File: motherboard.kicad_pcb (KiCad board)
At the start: 2 copper layers, 100.9 x 70.4 mm, 153 parts, among them J1 USB_C_Receptacle_USB2.0, J10 Power input, J11 Bed, J12 Hotend, J13 X_LIMIT, J14 Y_LIMIT, J15 Z_LIMIT, J2 SWD, J3 EXP, J5 Conn_01x03, J6 FAN, J7 Conn_02x03_Odd_Even, J8 BED_TEMP, J9 HOTEND_TEMP, M1 NEMA17, M2 NEMA17, M3 NEMA17, M4 NEMA17, Q1 BC847, Q2 BC847, Q3 AO3400A, Q5 APM4010, Q6 APM4010, U1 MP1584, U2 STM32F103C8Tx, U3 AMS1117-3.3, U4 A4988, U5 A4988, U6 A4988, U7 A4988, U8 CH340E, Y1 8MHz

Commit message: change PCB design
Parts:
- removed the C50 at (121.2, 121.4)
- removed the C51 at (120.7, 124.2)
- removed the C52 at (113.3, 121.4)
- removed the D5 at (113.3, 128.9)
- removed D7: LED, LED_SMD:LED_0603_1608Metric_Pad1.05x0.95mm_HandSolder
- removed the R24 at (82.8, 117.4)
- removed the R26 at (103.2, 117.5)
- removed the R40 at (115.7, 125.1)
- removed the R54 at (117.7, 114.7)
- removed the REF** at (64.2, 133.8)
- removed the U2 at (99.2, 140.0)
- added C3: 4u7, Capacitor_SMD:C_0603_1608Metric_Pad1.08x0.95mm_HandSolder, F.Cu at (102.5, 146.1)
- added C35: 1n, Capacitor_SMD:C_0603_1608Metric_Pad1.08x0.95mm_HandSolder, F.Cu at (126.8, 111.8)
- added C36: 1n, Capacitor_SMD:C_0603_1608Metric_Pad1.08x0.95mm_HandSolder, F.Cu at (123.2, 125.0)
- added C41: 1u, Capacitor_SMD:C_0603_1608Metric_Pad1.08x0.95mm_HandSolder, F.Cu at (121.2, 115.5)
- added D6: LED, LED_SMD:LED_0603_1608Metric_Pad1.05x0.95mm_HandSolder, F.Cu at (117.7, 125.5)
- added GND: TestPoint_Loop_D1.80mm_Drill1.0mm_Beaded, TestPoint:TestPoint_Loop_D1.80mm_Drill1.0mm_Beaded, F.Cu at (41.4, 152.5)
- added J10: 5V, Connector_PinHeader_2.54mm:PinHeader_2x02_P2.54mm_Vertical, F.Cu at (63.5, 128.5)
- added JP1: UART, Jumper:SolderJumper-2_P1.3mm_Open_TrianglePad1.0x1.5mm, F.Cu at (103.4, 128.0)
- added QR*****: QR_signed, Footprints:QR_signed, B.Cu at (51.2, 136.2)
- added R1: 1m, Resistor_SMD:R_0603_1608Metric_Pad0.98x0.95mm_HandSolder, F.Cu at (89.3, 136.3)
- added R16: 10k, Resistor_SMD:R_0402_1005Metric_Pad0.72x0.64mm_HandSolder, F.Cu at (43.5, 116.8)
- added R17: 10k, Resistor_SMD:R_0402_1005Metric_Pad0.72x0.64mm_HandSolder, F.Cu at (65.2, 116.6)
- added R18: 10k, Resistor_SMD:R_0402_1005Metric_Pad0.72x0.64mm_HandSolder, F.Cu at (85.5, 116.6)
- added R19: 10k, Resistor_SMD:R_0402_1005Metric_Pad0.72x0.64mm_HandSolder, F.Cu at (106.0, 117.0)
- added R21: 10k, Resistor_SMD:R_0402_1005Metric_Pad0.72x0.64mm_HandSolder, F.Cu at (61.3, 117.2)
- added R23: 10k, Resistor_SMD:R_0402_1005Metric_Pad0.72x0.64mm_HandSolder, F.Cu at (102.0, 117.5)
- added R28: 10k, Resistor_SMD:R_0402_1005Metric_Pad0.72x0.64mm_HandSolder, F.Cu at (41.7, 117.4)
- added R30: 10k, Resistor_SMD:R_0402_1005Metric_Pad0.72x0.64mm_HandSolder, F.Cu at (63.5, 117.2)
- added R32: 10k, Resistor_SMD:R_0402_1005Metric_Pad0.72x0.64mm_HandSolder, F.Cu at (83.7, 117.2)
- added R34: 10k, Resistor_SMD:R_0402_1005Metric_Pad0.72x0.64mm_HandSolder, F.Cu at (104.2, 117.6)
- added R4: 10k, Resistor_SMD:R_0402_1005Metric_Pad0.72x0.64mm_HandSolder, F.Cu at (106.0, 118.2)
- added R5: 10k, Resistor_SMD:R_0402_1005Metric_Pad0.72x0.64mm_HandSolder, F.Cu at (38.4, 117.4)
- added R50: 1k, Resistor_SMD:R_0603_1608Metric_Pad0.98x0.95mm_HandSolder, F.Cu at (120.3, 122.9)
- added R6: 10k, Resistor_SMD:R_0402_1005Metric_Pad0.72x0.64mm_HandSolder, F.Cu at (60.2, 117.2)
- added R7: 10k, Resistor_SMD:R_0402_1005Metric_Pad0.72x0.64mm_HandSolder, F.Cu at (80.4, 117.2)
- added REF**: MountingHole_3.2mm_M3_ISO14580, MountingHole:MountingHole_3.2mm_M3_ISO14580, F.Cu at (64.2, 133.8)
- added U1: STM32F401CCUx, Package_DFN_QFN:QFN-48-1EP_7x7mm_P0.5mm_EP5.6x5.6mm, F.Cu at (99.2, 140.0)
- M1, M2, M3, M4: footprint Connector_JST:JST_EH_B4B-EH-A_1x04_P2.50mm_Vertical -> Connector_JST:JST_XH_B4B-XH-A_1x04_P2.50mm_Vertical
- R10, R11, R12, R13, R14, R15, R20, R22, R8, R9: footprint Resistor_SMD:R_0603_1608Metric_Pad0.98x0.95mm_HandSolder -> Resistor_SMD:R_0402_1005Metric_Pad0.72x0.64mm_HandSolder
- U8: value CH340E -> USBLC6-2SC6; footprint Package_SO:MSOP-10_3x3mm_P0.5mm -> Package_TO_SOT_SMD:SOT-23-6
- moved R8 58.2 mm to (100.9, 117.5), turned to 270 degrees
- moved R14 39.8 mm to (65.2, 117.8), turned to 180 degrees
- moved R13 37.3 mm to (43.5, 118.0), turned to 180 degrees
- moved R3 24.5 mm to (105.5, 129.2), turned to 90 degrees
- moved R11 22.1 mm to (82.6, 117.2)
- moved R22 19.0 mm to (81.5, 117.2), turned to 270 degrees
- moved R12 18.7 mm to (103.1, 117.5), turned to 270 degrees
- moved R15 15.8 mm to (85.5, 117.8), turned to 180 degrees
- moved R2 4.90 mm to (96.1, 129.9), turned to 315 degrees
- moved C34 4.03 mm to (60.5, 127.5)
- moved C40 3.18 mm to (118.4, 146.4)
- moved C2 3.01 mm to (84.9, 136.5)
- moved Y1 3.01 mm to (87.2, 134.2)
- moved C1 3.01 mm to (89.5, 131.9)
- moved U8 2.33 mm to (116.7, 121.0), turned to 225 degrees
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- renumbered C17 to C10, C18 to C11, C19 to C12, C20 to C13, C21 to C14, C22 to C15, C23 to C16, C24 to C17, C25 to C18, C26 to C19, C27 to C20, C28 to C21, C29 to C22, C30 to C23, C31 to C24, C32 to C25, C33 to C26, C34 to C27, C35 to C28, C36 to C29, C37 to C30, C38 to C31, C39 to C32, C40 to C33, C7 to C34, C9 to C37, C3 to C38, C10 to C39, C11 to C40, C6 to C42, C8 to C43, C48 to C44, C12 to C45, C43 to C46, C44 to C47, C41 to C48, C42 to C49, C45 to C50, C46 to C51, C47 to C52, C13 to C6, C14 to C7, C15 to C8, C16 to C9, D6 to D4, D4 to D5, J2 to J1, J1 to J2, J5 to J4, J8 to J5, J9 to J6, J6 to J7, J10 to J8, J7 to J9, Q5 to Q4, Q6 to Q5, R52 to R2, R16 to R24, R17 to R25, R18 to R26, R19 to R27, R21 to R29, R53 to R3, R23 to R31, R25 to R33, R27 to R35, R28 to R36, R29 to R37, R30 to R38, R31 to R39, R32 to R40, R33 to R41, R34 to R42, R35 to R43, R1 to R44, R2 to R45, R3 to R46, R4 to R47, R5 to R48, R51 to R49, R6 to R51, R7 to R52, R45 to R53, R46 to R54, R36 to R55, R37 to R56, R38 to R57, R39 to R58, R41 to R59, R42 to R60, R44 to R61, R47 to R62, R48 to R63, R49 to R64, R50 to R65, U4 to U2, U5 to U3, U6 to U4, U7 to U5, U3 to U6, U1 to U7
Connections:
- net Net-(C1-Pad2) renamed /PH0
- net Net-(C2-Pad1) renamed /PH1
- GND pad 1: (no net) -> GND
- J1 pad 5: /PA13 -> /CS2
- J2 pad A6: /D+ -> Net-(J2-PadA6)
- J2 pad A7: /D- -> Net-(J2-PadA7)
- J2 pad B6: /D+ -> Net-(J2-PadA6)
- J2 pad B7: /D- -> Net-(J2-PadA7)
- J2 pad S1: GND -> Net-(C35-Pad1)
- J3 pad 10: /SCL -> /CS2
- J3 pad 8: /ENC_PUSH -> /CS
- J3 pad 9: /SDA -> /ENC_PUSH
- R10 pad 1: +3V3 -> Net-(R10-Pad1)
- R10 pad 2: Net-(R10-Pad2) -> +3V3
- R11 pad 1: +3V3 -> Net-(R11-Pad1)
- R11 pad 2: /Y_SLEEP -> +3V3
- R12 pad 1: +3V3 -> Net-(R12-Pad1)
- R12 pad 2: Net-(R12-Pad2) -> +3V3
- R13 pad 1: +3V3 -> Net-(R13-Pad1)
- R13 pad 2: /Z_SLEEP -> GND
- R14 pad 1: +3V3 -> Net-(R14-Pad1)
- R14 pad 2: Net-(R14-Pad2) -> GND
- R15 pad 1: +3V3 -> Net-(R15-Pad1)
- R15 pad 2: /E_SLEEP -> GND
- R20 pad 1: GND -> Net-(R20-Pad1)
- R20 pad 2: Net-(R20-Pad2) -> +3V3
- R22 pad 1: GND -> Net-(R22-Pad1)
- R22 pad 2: Net-(R22-Pad2) -> +3V3
- R8 pad 2: Net-(R8-Pad2) -> /E_SLEEP
- R9 pad 1: +3V3 -> Net-(R9-Pad1)
- R9 pad 2: /X_SLEEP -> +3V3
- U2 pad 11: +3V3 -> Net-(R20-Pad1)
- U2 pad 12: Net-(R8-Pad2) -> Net-(R9-Pad1)
- U2 pad 13: Net-(R20-Pad2) -> Net-(R28-Pad2)
- U2 pad 14: Net-(R8-Pad2) -> Net-(R13-Pad1)
- U3 pad 11: +3V3 -> Net-(R21-Pad1)
- U3 pad 12: Net-(R10-Pad2) -> Net-(R10-Pad1)
- U3 pad 13: Net-(R22-Pad2) -> Net-(R30-Pad2)
- U3 pad 14: Net-(R10-Pad2) -> Net-(R14-Pad1)
- U4 pad 11: +3V3 -> Net-(R22-Pad1)
- U4 pad 12: Net-(R12-Pad2) -> Net-(R11-Pad1)
- U4 pad 14: Net-(R12-Pad2) -> Net-(R15-Pad1)
- U5 pad 11: +3V3 -> Net-(R23-Pad1)
- U5 pad 12: Net-(R14-Pad2) -> Net-(R12-Pad1)
- U5 pad 14: Net-(R14-Pad2) -> Net-(JP1-Pad2)
- U8 pad 1: /D+ -> Net-(J2-PadA7)
- U8 pad 2: /D- -> GND
- U8 pad 3: GND -> Net-(J2-PadA6)
- U8 pad 4: Net-(C52-Pad1) -> /D+
- U8 pad 5: Net-(U8-Pad5) -> /PC_CONN
- U8 pad 6: Net-(R40-Pad1) -> /D-
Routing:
- net /CS2: track 0.00 -> 30.9 mm, vias 0 -> 1
- net +3V3: track 357.4 -> 387.2 mm, vias 17 -> 16
- net /SCL: track 29.5 -> 0.00 mm
- net /RX: track 28.9 -> 0.00 mm
- net /TX: track 28.1 -> 0.00 mm
- net /SDA: track 25.7 -> 0.00 mm
- net /CS: track 0.00 -> 25.0 mm
- net Net-(JP1-Pad2): track 0.00 -> 22.7 mm, vias 0 -> 2
- net /NRST: track 47.3 -> 27.6 mm, vias 3 -> 1
- net /D-: track 8.32 -> 26.0 mm
- net /D+: track 8.65 -> 25.6 mm
- net Net-(J2-PadA6): track 0.00 -> 11.1 mm
- net Net-(J2-PadA7): track 0.00 -> 9.46 mm
- net /E_DIR: track 47.3 -> 56.5 mm
- net Net-(R8-Pad2): track 8.33 -> 0.00 mm
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- added copper zone on F.Cu, net Net-(C35-Pad1)
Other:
- board size 100.9 x 70.4 mm -> 100 x 70.3 mm
- board text added: "+-"
- board text added: "+24"
- board text added: "+5V PA9 PB15 PB13 PB10 PB2 +3V3"
- board text added: "5V"
- board text added: "GND"
- board text added: "GND PA8 PB14 PB12 PA13 PB1 GND"
- board text added: "Perm Feb-Apr 2022"
- board text added: "STM32F401CСU6"
- board text removed: "@w8mepls"
- board text removed: "Perm February 2022"
- board text removed: "STM32F103C8T6"

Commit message: pcb fixes
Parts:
- C10, C11, C12, C13: value 0u22 -> 2u2
- C14, C15, C16, C17: value 0u1 -> 22n
- C45, L1: value 10u -> 22u
- C6, C7, C8, C9: value 0u22 -> 0u1
- D5: value D_Schottky -> SS34
- R24, R25, R26, R27: value R* -> 10k
- R29, R31, R33, R35: value R* -> 10k; footprint Potentiometer_SMD:Potentiometer_Bourns_3314J_Vertical -> Potentiometer_SMD:Potentiometer_Bourns_TC33X_Vertical
- R51: value R -> 210k
- R52: value R -> 40k2
- moved R33 0.92 mm to (90.4, 112.9), turned to 270 degrees
- moved R29 0.82 mm to (48.5, 112.8), turned to 270 degrees
- moved R35 0.72 mm to (110.7, 112.8), turned to 270 degrees
- moved R31 0.71 mm to (70.1, 112.9), turned to 270 degrees
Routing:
- net /X_DIR: track 71.6 -> 70.4 mm
- net /Z_DIR: track 36.5 -> 35.7 mm
- net /E_DIR: track 56.5 -> 55.8 mm
- net Net-(R26-Pad1): track 7.86 -> 7.24 mm
- net GND: vias 79 -> 78

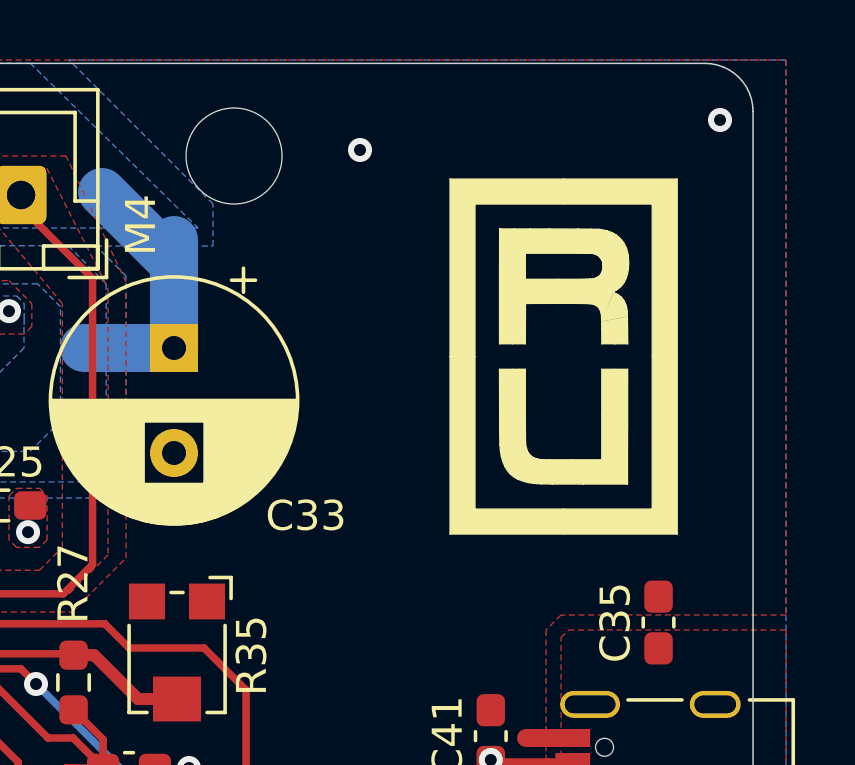
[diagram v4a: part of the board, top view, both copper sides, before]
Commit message: add logo to pcb
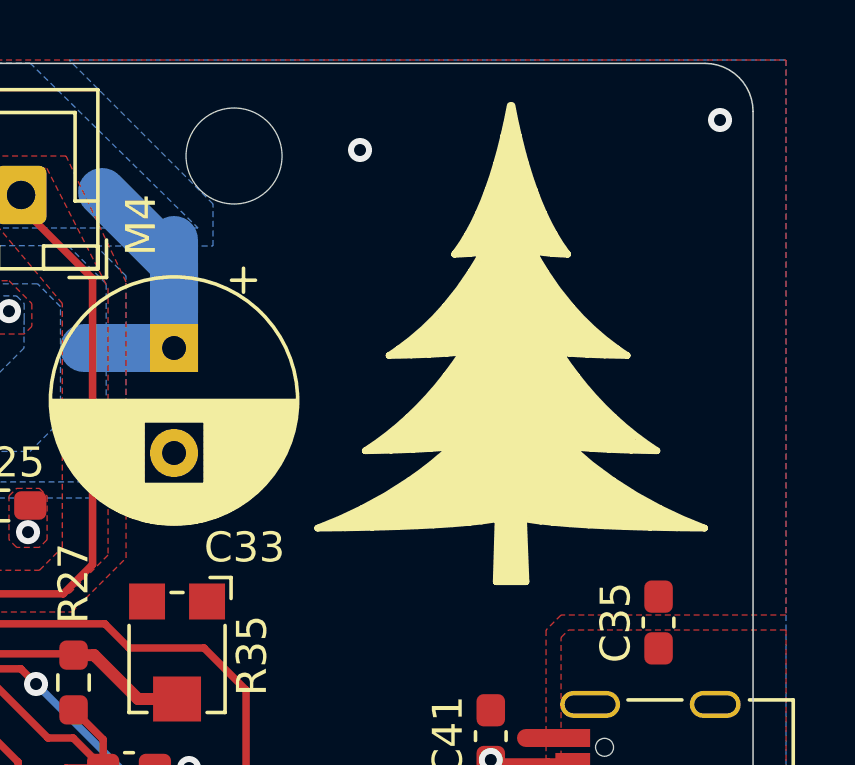
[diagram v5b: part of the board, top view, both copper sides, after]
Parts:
- removed the REF** at (119.8, 108.8)
- added REF**: spruce_fill, Footprints:spruce_fill, F.Cu at (121.8, 103.2)
